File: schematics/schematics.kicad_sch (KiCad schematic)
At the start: 9 parts, among them J3 2K, J4 POWER, U1 STM32F103VBT6, U2 AMS1117-3.3

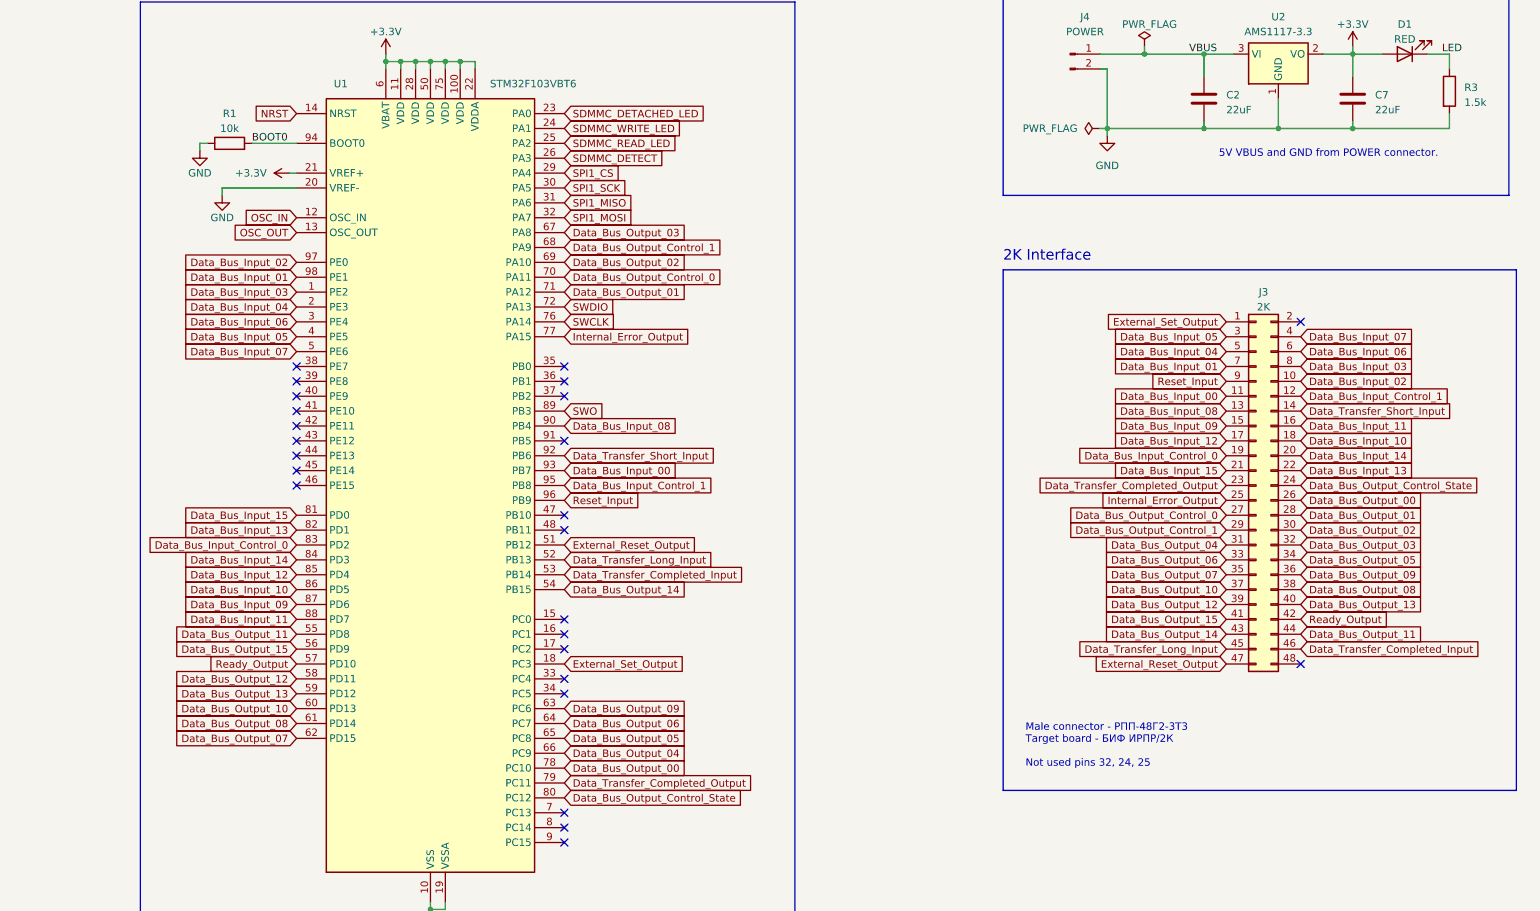
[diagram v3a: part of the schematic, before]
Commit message: Tune PCB trace spacing
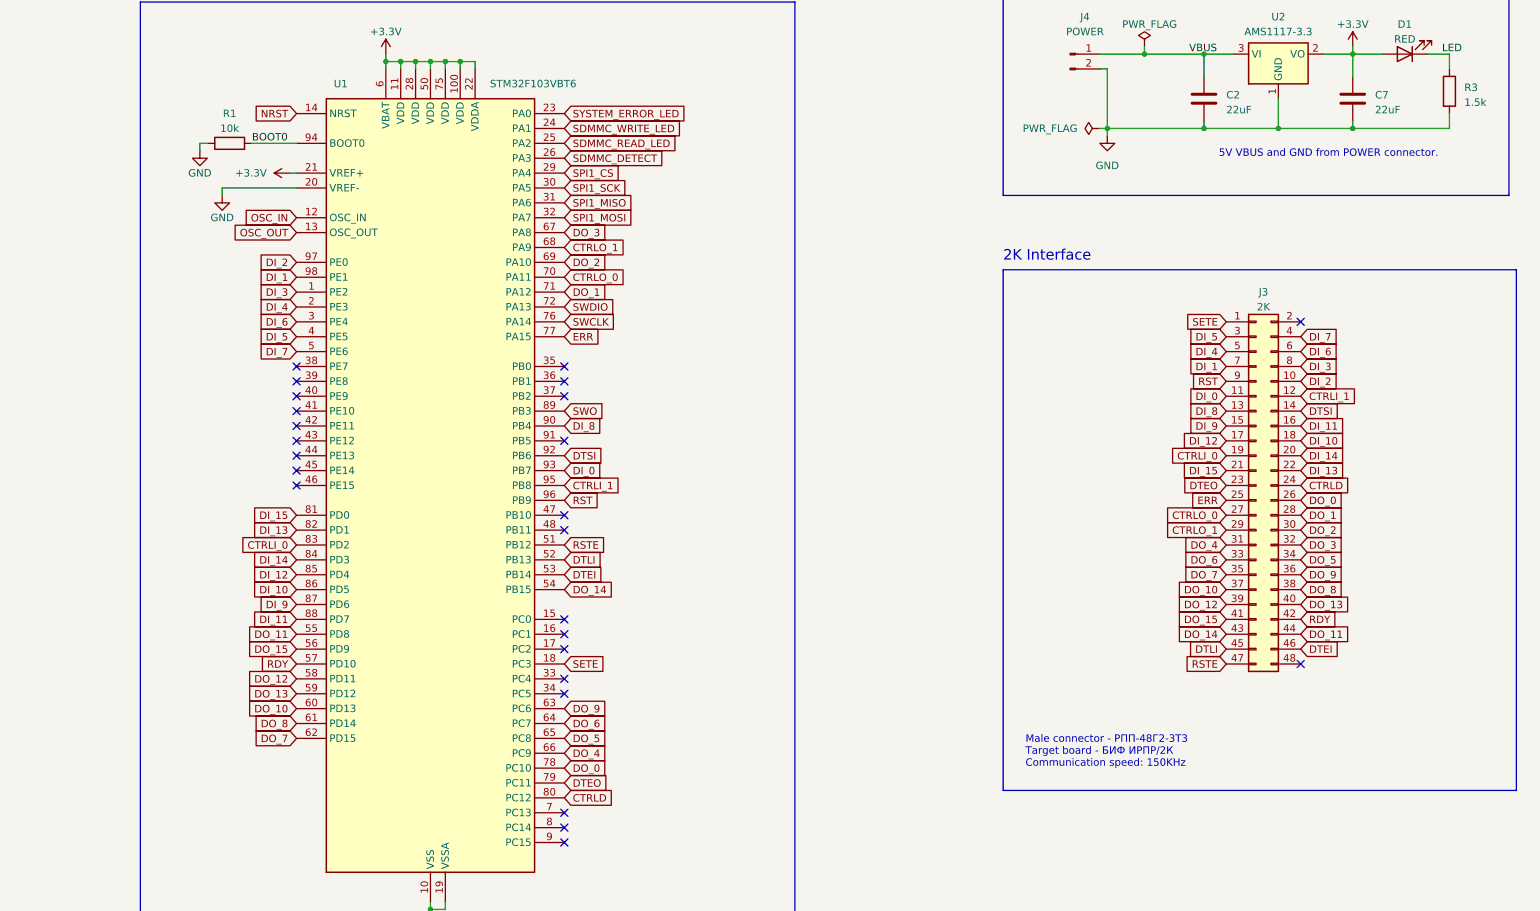
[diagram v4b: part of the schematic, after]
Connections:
- net Data_Bus_Input_00 renamed DI_0
- net Data_Bus_Input_01 renamed DI_1
- net Data_Bus_Input_02 renamed DI_2
- net Data_Bus_Input_03 renamed DI_3
- net Data_Bus_Input_04 renamed DI_4
- net Data_Bus_Input_05 renamed DI_5
- net Data_Bus_Input_06 renamed DI_6
- net Data_Bus_Input_07 renamed DI_7
- net Data_Bus_Input_08 renamed DI_8
- net Data_Bus_Input_09 renamed DI_9
- net Data_Bus_Input_10 renamed DI_10
- net Data_Bus_Input_11 renamed DI_11
- net Data_Bus_Input_12 renamed DI_12
- net Data_Bus_Input_13 renamed DI_13
- net Data_Bus_Input_14 renamed DI_14
- net Data_Bus_Input_15 renamed DI_15
- net Data_Bus_Input_Control_0 renamed CTRLI_0
- net Data_Bus_Input_Control_1 renamed CTRLI_1
- net Data_Bus_Output_00 renamed DO_0
- net Data_Bus_Output_01 renamed DO_1
- net Data_Bus_Output_02 renamed DO_2
- net Data_Bus_Output_03 renamed DO_3
- net Data_Bus_Output_04 renamed DO_4
- net Data_Bus_Output_05 renamed DO_5
- net Data_Bus_Output_06 renamed DO_6
- net Data_Bus_Output_07 renamed DO_7
- net Data_Bus_Output_08 renamed DO_8
- net Data_Bus_Output_09 renamed DO_9
- net Data_Bus_Output_10 renamed DO_10
- net Data_Bus_Output_11 renamed DO_11
- net Data_Bus_Output_12 renamed DO_12
- net Data_Bus_Output_13 renamed DO_13
- net Data_Bus_Output_14 renamed DO_14
- net Data_Bus_Output_15 renamed DO_15
- net Data_Bus_Output_Control_0 renamed CTRLO_0
- net Data_Bus_Output_Control_1 renamed CTRLO_1
- net Data_Bus_Output_Control_State renamed CTRLD
- net Data_Transfer_Completed_Input renamed DTEI
- net Data_Transfer_Completed_Output renamed DTEO
- net Data_Transfer_Long_Input renamed DTLI
- net Data_Transfer_Short_Input renamed DTSI
- net External_Reset_Output renamed RSTE
- net External_Set_Output renamed SETE
- net Internal_Error_Output renamed ERR
- net Ready_Output renamed RDY
- net Reset_Input renamed RST
- net SDMMC_DETACHED_LED renamed SYSTEM_ERROR_LED
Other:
- note added: "Male connector - РПП-48Г2-3Т3 Target board - БИФ ИРПР/2К Communication speed: 150KHz"
- note removed: "Male connector - РПП-48Г2-3Т3 Target board - БИФ ИРПР/2К Not used pins 32, 24, 25"

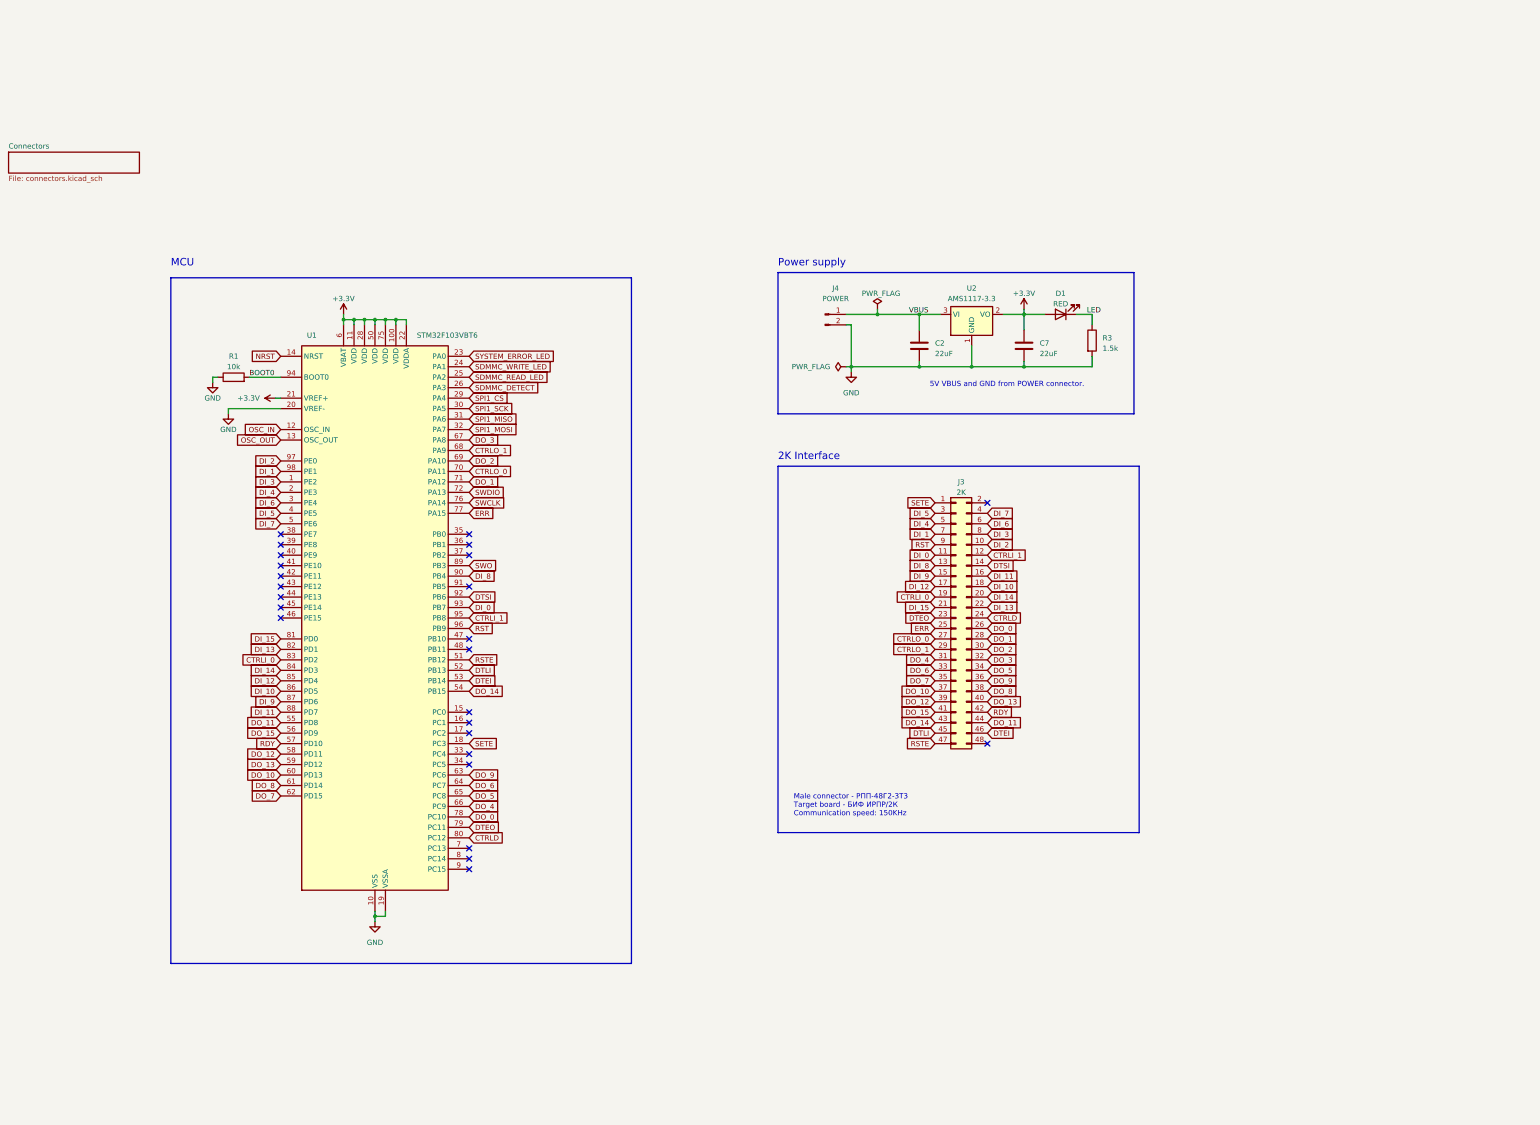
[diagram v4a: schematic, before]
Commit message: Move components to appropriate sheets
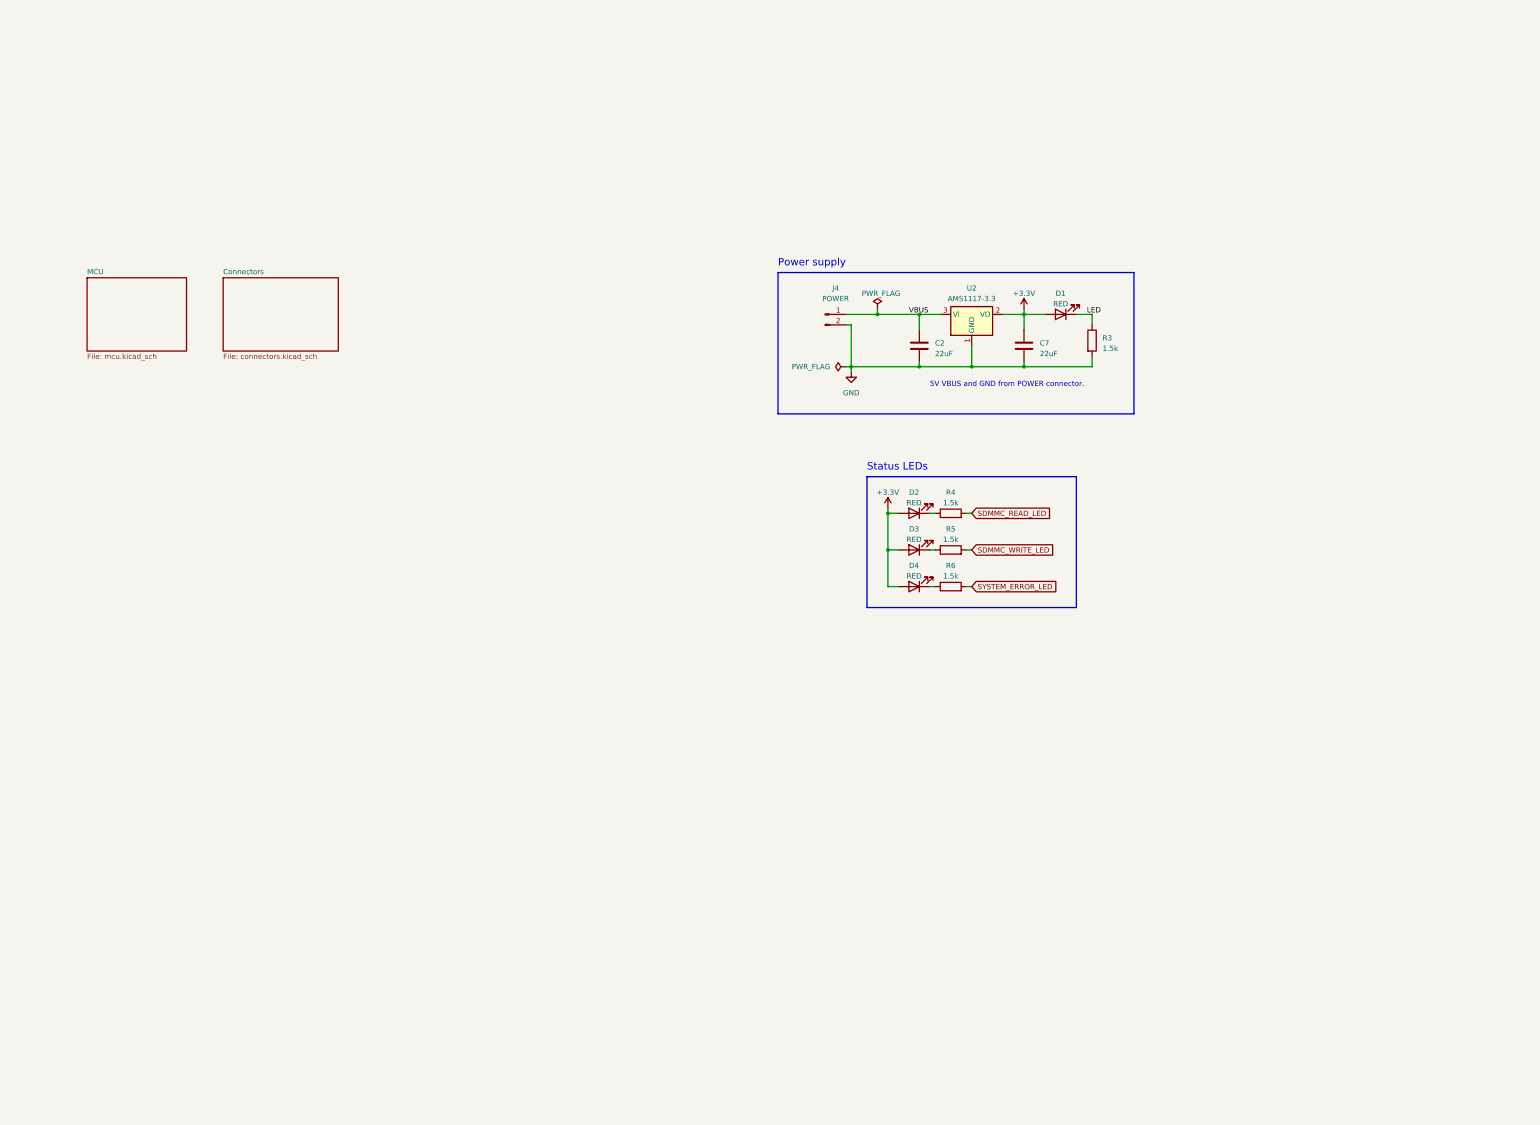
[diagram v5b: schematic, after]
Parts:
- removed J3: 2K, Custom:RPP_48G2_3T3_Male, symbol Connector_Generic:Conn_02x24_Odd_Even
- removed R1: 10k, Resistor_SMD:R_0603_1608Metric, symbol Device:R
- removed U1: STM32F103VBT6, Package_QFP:LQFP-100_14x14mm_P0.5mm, symbol MCU_ST_STM32F1:STM32F103VBTx
- added D2, D3, D4: RED, LED_SMD:LED_0603_1608Metric, symbol Device:LED
- added R4, R5, R6: 1.5k, Resistor_SMD:R_0603_1608Metric, symbol Device:R
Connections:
- net +3.3V: now also D2.2 (A), D3.2 (A), D4.2 (A)
- net SDMMC_READ_LED: now also R4.2
- net SDMMC_WRITE_LED: now also R5.2
- net SYSTEM_ERROR_LED: now also R6.2
- new net: D2.1 (K), R4.1
- new net: D4.1 (K), R6.1
- new net: D3.1 (K), R5.1
- no-connect marks 25 -> 0
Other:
- added sheet MCU (mcu.kicad_sch)
- note added: "Status LEDs"
- note removed: "2K Interface"
- note removed: "MCU"
- note removed: "Male connector - РПП-48Г2-3Т3 Target board - БИФ ИРПР/2К Communication speed: 150KHz"

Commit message: Update documentation
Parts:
- removed C2, C7: 22uF, Capacitor_SMD:C_0603_1608Metric, symbol Device:C
- removed D1: RED, LED_SMD:LED_0603_1608Metric, symbol Device:LED
- removed J4: POWER, Connector_JST:JST_EH_B2B-EH-A_1x02_P2.50mm_Vertical, symbol Connector:Conn_01x02_Pin
- removed R3: 1.5k, Resistor_SMD:R_0603_1608Metric, symbol Device:R
- removed U2: AMS1117-3.3, Package_TO_SOT_SMD:SOT-223-3_TabPin2, symbol Regulator_Linear:AMS1117-3.3
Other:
- added sheet Power (pwr.kicad_sch)
- note removed: "5V VBUS and GND from POWER connector."
- note removed: "Power supply"
